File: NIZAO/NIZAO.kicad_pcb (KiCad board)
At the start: 4 copper layers, 107 x 87.7 mm, 180 parts, among them J1 Screw_Terminal_01x09, J2 Screw_Terminal_01x09, J3 Screw_Terminal_01x09, J4 Screw_Terminal_01x09, J5 PZ254R-12-14P, K1 G5V-1, K2 G5V-1, Q1 NCE60P04R, Q2 ZXMS6004FFQTA, Q3 ZXMS6004FFQTA, Q4 ZXMS6004FFQTA, Q5 ZXMS6004FFQTA, SW1 TS-1088-AR02016, U1 ADS1115IDGS, U10 AT3H4B-CUH-S, U11 MAX31856MUD+, U12 BL0942, U13 B0303S-1WR3_C7465185, U14 ISO7021DR, U15 GP8211S-TC50-EW, U16 GP8302-TC50-EW, U17 BTS723GWXUMA1, U18 LK1802, U2 ESP32-S3-WROOM-1, U3 RS485-PROTECT, U4 AP63203WU, U5 AT3H4B-CUH-S, U6 AT3H4B-CUH-S, U7 AT3H4B-CUH-S, U8 AT3H4B-CUH-S, U9 AT3H4B-CUH-S

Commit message: actualizado
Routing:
- net /BoardNIZAO/OUT_RLY2: track 12.3 -> 14.6 mm, vias 0 -> 2
- net /BoardNIZAO/IN_NPN1: track 116.2 -> 117.4 mm, vias 2 -> 0
- net /BoardNIZAO/cs: track 80.1 -> 79.0 mm
- net /BoardNIZAO/OUT_PNP2: track 33.7 -> 32.6 mm, vias 0 -> 2
- net /BoardNIZAO/IN_NPN4: track 105.6 -> 106.5 mm
- net /BoardNIZAO/OUT_NPN4: track 57.7 -> 56.9 mm, vias 2 -> 0
- net /BoardNIZAO/OUT_NPN1: track 60.1 -> 60.9 mm, vias 2 -> 0
- net /BoardNIZAO/OUT_NPN2: track 58.5 -> 59.0 mm, vias 2 -> 0
- net /BoardNIZAO/OUT_PNP1: vias 0 -> 2
- net /BoardNIZAO/OUT_NPN3: vias 2 -> 0

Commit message: actualizacion
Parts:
- moved C8 4.52 mm to (102.4, 85.3)
- moved L1 2.38 mm to (105.9, 79.9)
- moved J1 0.22 mm to (108.7, 59.8)
- moved J2 0.15 mm to (154.5, 59.7)
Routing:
- net /PawerSupply/sw: track 8.49 -> 10.1 mm
- net Net-(U4-BST): track 14.0 -> 13.2 mm
- net +3.3V: vias 42 -> 52
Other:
- board size 107 x 87.7 mm -> 102 x 82.8 mm

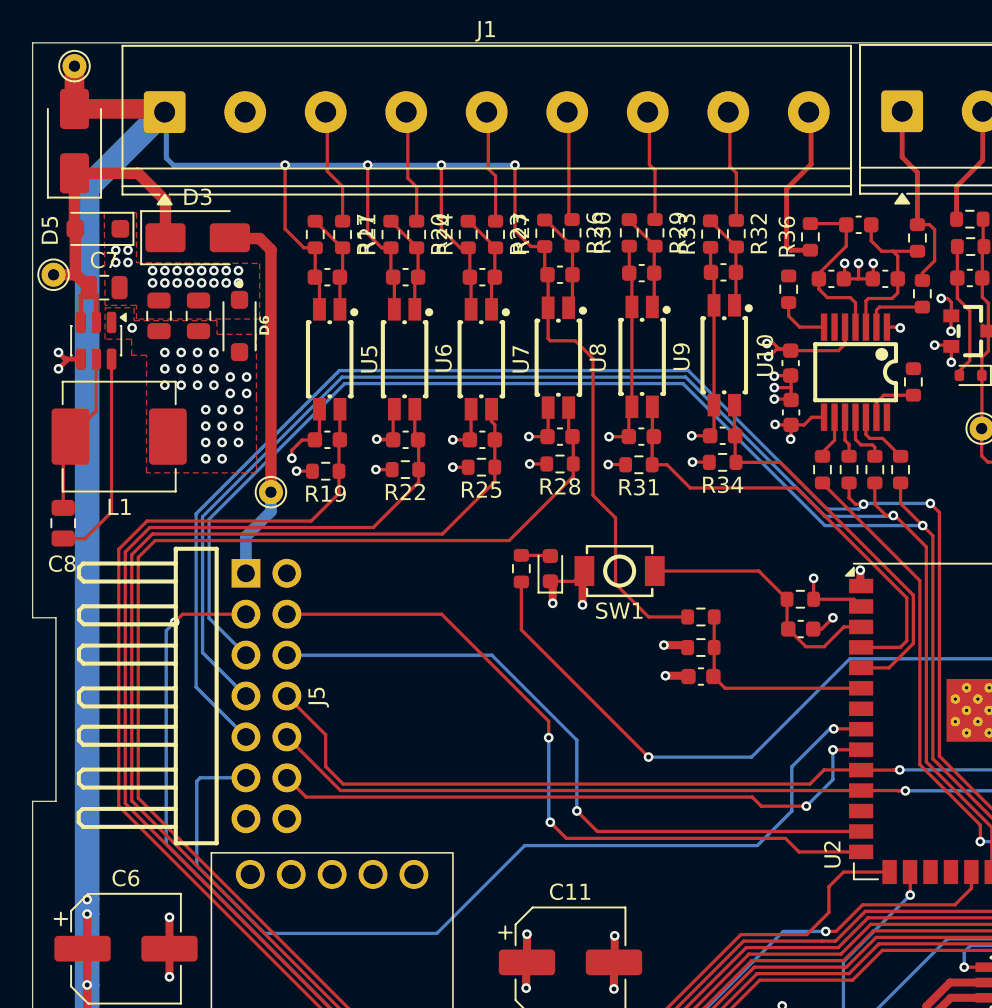
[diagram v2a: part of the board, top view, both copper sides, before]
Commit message: Actualiza el mezzanine, eliminar assembly de prueba y actualizar essembly
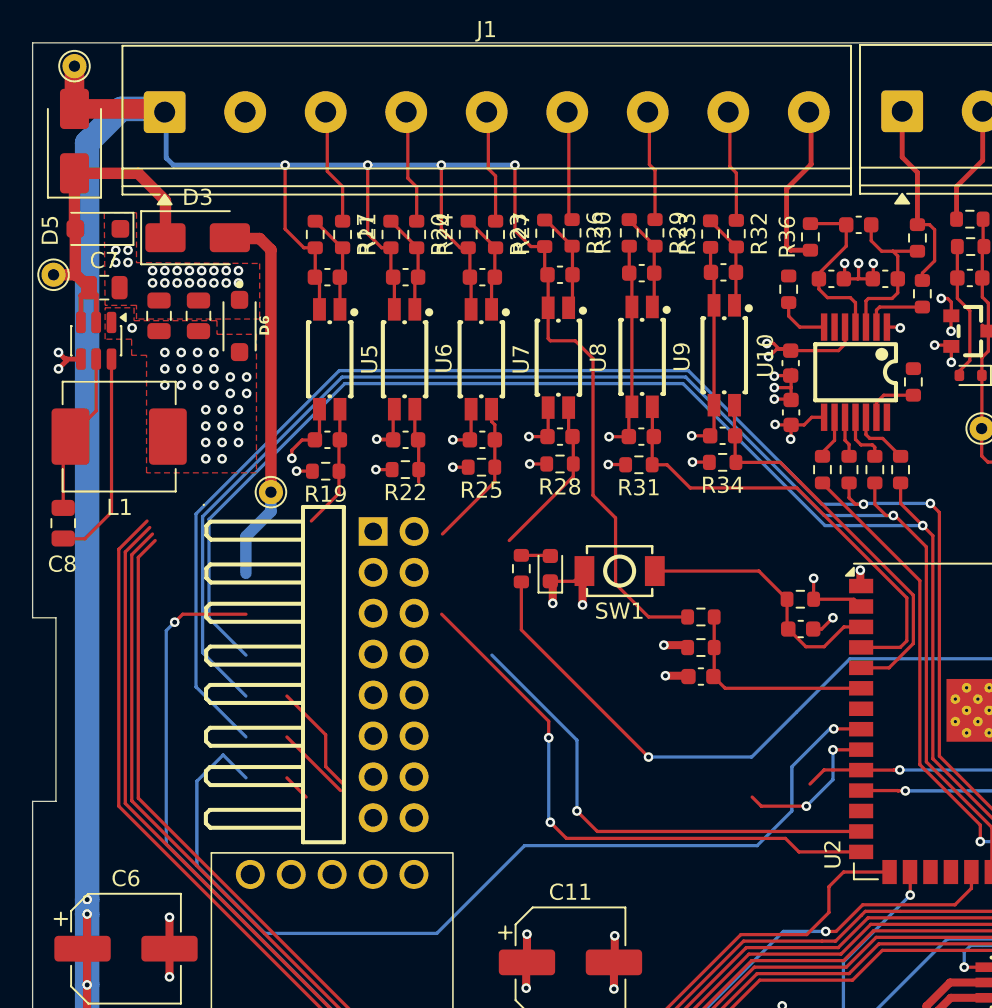
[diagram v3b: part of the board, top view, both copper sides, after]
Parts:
- removed J5: PZ254R-12-14P, XFCN PZ254R-12-14P:HDR-TH_14P-P2.54-H-M-R2-C7-S2.54
- added H3: PZ254R-12-16P, EasyEDA:HDR-TH_16P-P2.54-H-M-R2-C8-S2.54, F.Cu at (122.9, 94.7)
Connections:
- C17 pad 1: Net-(C17-Pad1) -> Net-(U19-AN/CAT)
- C19 pad 1: Net-(C19-Pad1) -> Net-(U20-AN/CAT)
- C21 pad 1: Net-(C21-Pad1) -> Net-(U21-AN/CAT)
- C23 pad 1: Net-(C23-Pad1) -> Net-(U22-AN/CAT)
- C25 pad 1: Net-(C25-Pad1) -> Net-(U23-AN/CAT)
- C27 pad 1: Net-(C27-Pad1) -> Net-(U24-AN/CAT)
- R17 pad 2: Net-(C17-Pad1) -> Net-(U19-AN/CAT)
- R18 pad 2: Net-(C17-Pad1) -> Net-(U19-AN/CAT)
- R20 pad 2: Net-(C19-Pad1) -> Net-(U20-AN/CAT)
- R21 pad 2: Net-(C19-Pad1) -> Net-(U20-AN/CAT)
- R23 pad 2: Net-(C21-Pad1) -> Net-(U21-AN/CAT)
- R24 pad 2: Net-(C21-Pad1) -> Net-(U21-AN/CAT)
- R26 pad 2: Net-(C23-Pad1) -> Net-(U22-AN/CAT)
- R27 pad 2: Net-(C23-Pad1) -> Net-(U22-AN/CAT)
- R29 pad 2: Net-(C25-Pad1) -> Net-(U23-AN/CAT)
- R30 pad 2: Net-(C25-Pad1) -> Net-(U23-AN/CAT)
- R32 pad 2: Net-(C27-Pad1) -> Net-(U24-AN/CAT)
- R33 pad 2: Net-(C27-Pad1) -> Net-(U24-AN/CAT)
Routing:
- net /BoardNIZAO/i2c_scl: track 120.9 -> 88.6 mm
- net /BoardNIZAO/i2c_sda: track 122.0 -> 93.1 mm
- net /BoardNIZAO/GPIO2: track 38.9 -> 11.2 mm
- net /BoardNIZAO/IN_NPN4: track 106.5 -> 84.5 mm
- net /BoardNIZAO/IN_NPN3: track 143.2 -> 125.1 mm
- net /BoardNIZAO/IN_NPN2: track 142.1 -> 124.2 mm
- net /BoardNIZAO/usb-: track 42.8 -> 30.0 mm
- net /BoardNIZAO/IN_NPN1: track 117.4 -> 107.2 mm
- net /BoardNIZAO/usb+: track 45.4 -> 35.8 mm
- net +24V: track 354.0 -> 355.6 mm
- net /BoardNIZAO/GPIO1: track 58.2 -> 59.4 mm

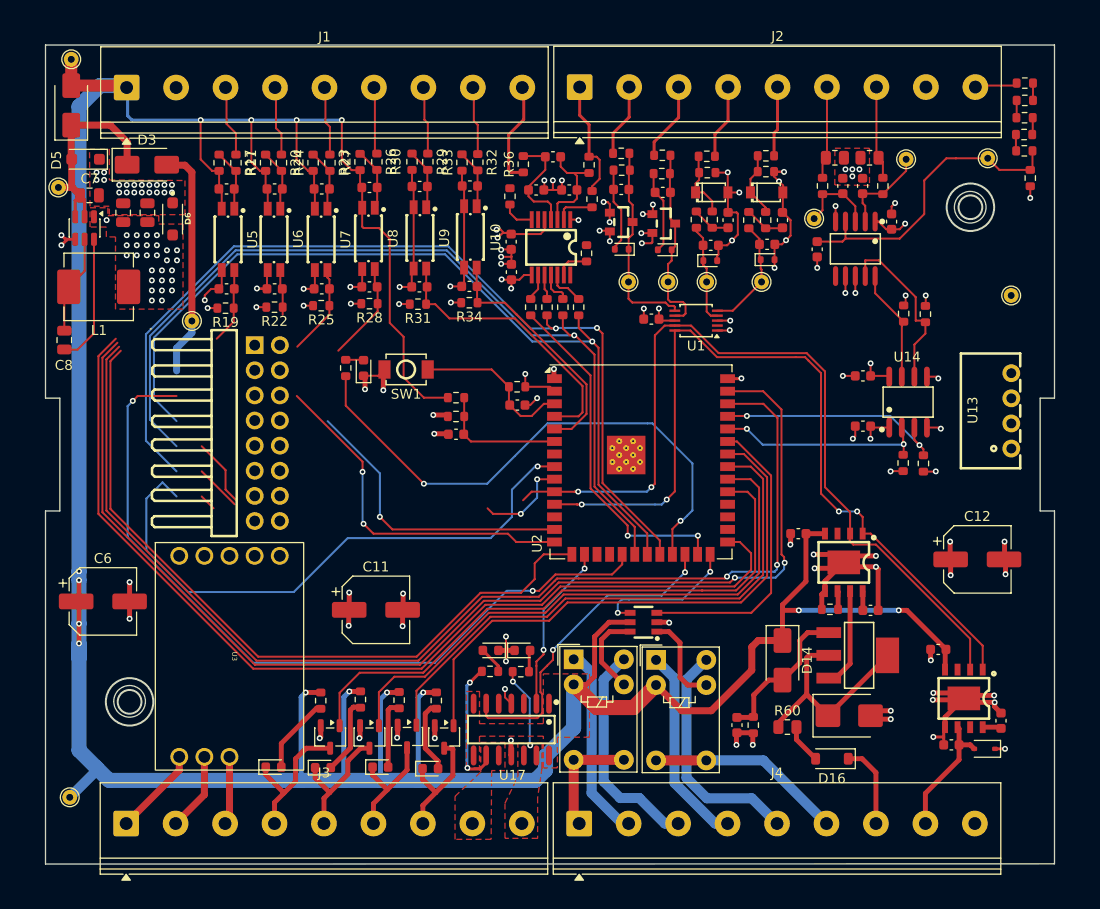
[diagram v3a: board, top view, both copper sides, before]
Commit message: Colocandos los 3d de los componetes en la placa NIZAO
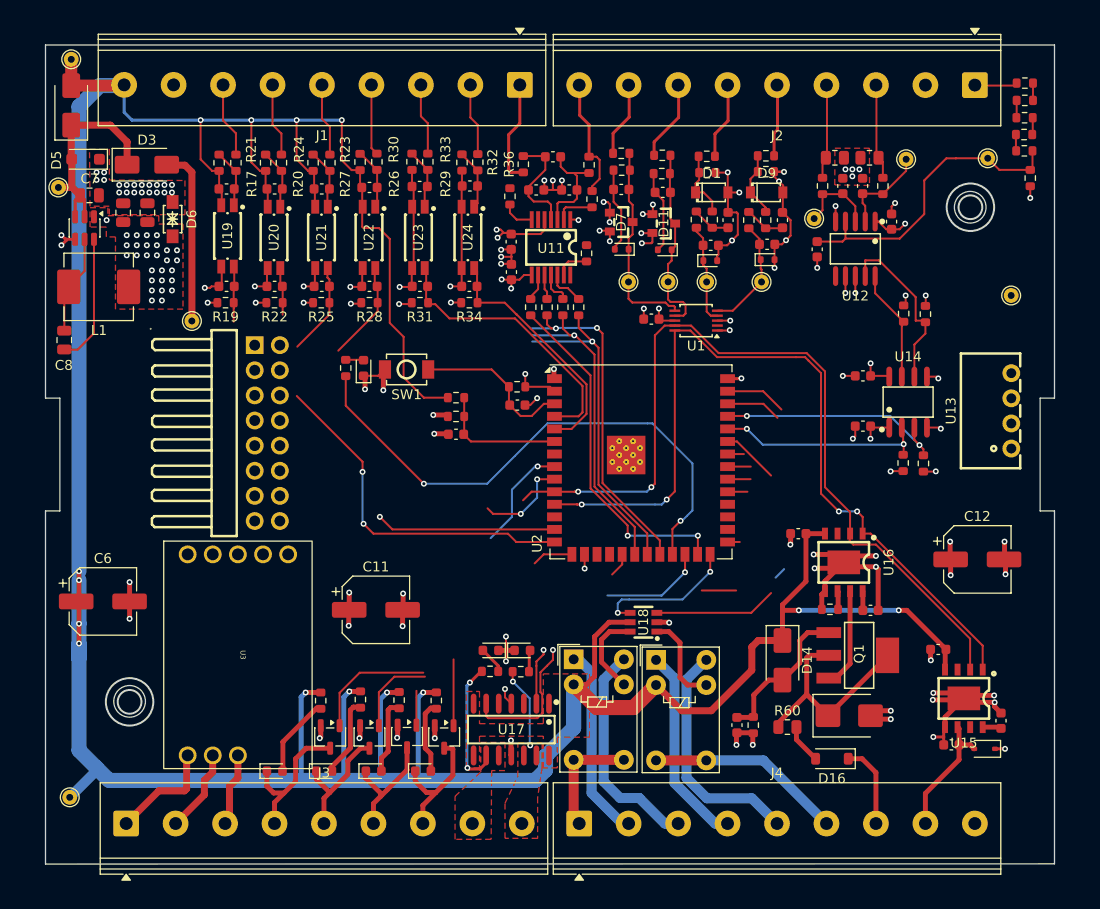
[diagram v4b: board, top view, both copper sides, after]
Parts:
- removed U10, U5, U6, U7, U8, U9: AT3H4B-CUH-S, AOTE AT3H4B-CuH-S:SSOP-4_L2.7-W4.6-P1.27-LS7.0-TL
- added U19: AT3H4B-CUH-S, JLCImport:AT3H4B-CUH-S, F.Cu at (118.9, 74.8)
- added U20: AT3H4B-CUH-S, JLCImport:AT3H4B-CUH-S, F.Cu at (123.6, 74.9)
- added U21: AT3H4B-CUH-S, JLCImport:AT3H4B-CUH-S, F.Cu at (128.4, 74.9)
- added U22: AT3H4B-CUH-S, JLCImport:AT3H4B-CUH-S, F.Cu at (133.2, 74.9)
- added U23: AT3H4B-CUH-S, JLCImport:AT3H4B-CUH-S, F.Cu at (138.2, 74.9)
- added U24: AT3H4B-CUH-S, JLCImport:AT3H4B-CUH-S, F.Cu at (143.2, 74.9)
- D1, D9: footprint DIODES 1N5819HW-7-F:SOD-123_L2.7-W1.6-LS3.7-RD -> JLCImport:1N5819HW-7-F
- D11, D7: footprint DIODES BAT54S-7-F:SOT-23_L2.9-W1.3-P1.90-LS2.4-BR -> JLCImport:BAT54S-7-F
- D6: footprint SMF3.3_SODFL3718X108N:SMF3.3_SODFL3718X108N -> JLCImport:SMF3_3CA_C6165153
- Q1: footprint NCE NCE60P04R:SOT-223-3_L6.5-W3.4-P2.30-LS7.0-BR -> JLCImport:NCE60P04R
- SW1: footprint XUNPU TS-1088-AR02016:SW-SMD_L3.9-W3.0-P4.45 -> JLCImport:TS-1088-AR02016
- U11: footprint MAXIM MAX31856MUD+:TSSOP-14_L5.0-W4.4-P0.65-LS6.4-BL -> JLCImport:MAX31856MUD
- U12: footprint BL BL0942:SSOP-10_L4.9-W3.9-P1.00-LS6.0-BL -> JLCImport:BL0942
- U13: footprint EVISUN B0303S-1WR3:PWRM-TH_BXXXXS-1WR3 -> JLCImport:B0303S-1WR3_C7465185
- U14: footprint TI ISO7021DR:SOIC-8_L4.9-W3.9-P1.27-LS6.0-BL -> JLCImport:ISO7021DR
- U15: footprint Guestgood GP8211S-TC50-EW:ESOP-8_L4.9-W3.9-P1.27-LS6.0-BL-EP -> JLCImport:GP8211S-TC50-EW
- U16: footprint Guestgood GP8211S-TC50-EW:ESOP-8_L4.9-W3.9-P1.27-LS6.0-BL-EP -> JLCImport:GP8302-TC50-EW
- U17: footprint Infineon BTS723GW:SOIC-14_L8.7-W3.9-P1.27-LS6.0-BL -> JLCImport:BTS723GWXUMA1
- U18: footprint LANKE LK1802:SOT-23-6_L2.9-W1.6-P0.95-LS2.8-BR -> JLCImport:LK1802
- moved J2 40.0 mm to (194.4, 59.5), turned to 180 degrees
- moved J1 39.8 mm to (148.4, 59.5), turned to 180 degrees
- moved U3 0.86 mm to (120.0, 117.1)
- moved LED6 0.79 mm to (133.7, 128.8)
- moved LED7 0.77 mm to (138.7, 128.8)
- moved R19 0.55 mm to (118.7, 81.5)
- moved R22 0.45 mm to (123.7, 81.5)
- moved LED4 0.42 mm to (123.7, 128.8)
- moved LED5 0.37 mm to (128.7, 128.8)
- moved R25 0.30 mm to (128.4, 81.5)
- moved C18 0.25 mm to (118.8, 79.8)
- moved C20 0.25 mm to (123.7, 79.8)
- moved C22 0.25 mm to (128.4, 79.8)
- moved R31 0.25 mm to (138.3, 81.5)
- moved R28 0.10 mm to (133.2, 81.5)
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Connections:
- J1 pad 1: +24V -> /BoardNIZAO/CON_IN_TC+
- J1 pad 2: GND -> /BoardNIZAO/CON_IN_PNP2
- J1 pad 3: /BoardNIZAO/CON_IN_NPN1 -> /BoardNIZAO/CON_IN_PNP1
- J1 pad 4: /BoardNIZAO/CON_IN_NPN2 -> /BoardNIZAO/CON_IN_NPN4
- J1 pad 6: /BoardNIZAO/CON_IN_NPN4 -> /BoardNIZAO/CON_IN_NPN2
- J1 pad 7: /BoardNIZAO/CON_IN_PNP1 -> /BoardNIZAO/CON_IN_NPN1
- J1 pad 8: /BoardNIZAO/CON_IN_PNP2 -> GND
- J1 pad 9: /BoardNIZAO/CON_IN_TC+ -> +24V
- J2 pad 1: /BoardNIZAO/CON_IN_TC- -> /BoardNIZAO/CON-IN_VAC_P
- J2 pad 2: /BoardNIZAO/CON_IN_0-10V_1 -> Earth
- J2 pad 3: /BoardNIZAO/CON_IN_0-10V_2 -> /BoardNIZAO/CON-IN_CT_P
- J2 pad 4: /BoardNIZAO/CON-IN-4-20MA_1 -> /BoardNIZAO/CON-IN_CT_N
- J2 pad 6: /BoardNIZAO/CON-IN_CT_N -> /BoardNIZAO/CON-IN-4-20MA_1
- J2 pad 7: /BoardNIZAO/CON-IN_CT_P -> /BoardNIZAO/CON_IN_0-10V_2
- J2 pad 8: Earth -> /BoardNIZAO/CON_IN_0-10V_1
- J2 pad 9: /BoardNIZAO/CON-IN_VAC_P -> /BoardNIZAO/CON_IN_TC-
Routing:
- net /BoardNIZAO/IN_NPN2: track 124.2 -> 12.1 mm, vias 2 -> 0
- net /BoardNIZAO/IN_NPN3: track 125.1 -> 14.8 mm, vias 2 -> 0
- net /BoardNIZAO/IN_NPN1: track 107.2 -> 6.49 mm
- net /BoardNIZAO/cs: track 79.0 -> 2.46 mm, vias 2 -> 0
- net /BoardNIZAO/IN_NPN4: track 84.5 -> 14.2 mm
- net /BoardNIZAO/clk: track 95.4 -> 34.3 mm
- net /BoardNIZAO/miso: track 89.8 -> 31.8 mm
- net /BoardNIZAO/mosi: track 87.9 -> 33.1 mm
- net /BoardNIZAO/OUT_NPN3: track 57.2 -> 5.83 mm
- net /BoardNIZAO/OUT_NPN4: track 56.9 -> 8.36 mm
- net /BoardNIZAO/GPIO1: track 59.4 -> 11.1 mm
- net /BoardNIZAO/OUT_NPN2: track 59.0 -> 11.0 mm
- net /BoardNIZAO/OUT_NPN1: track 60.9 -> 18.1 mm
- net /BoardNIZAO/OUT_RLY1: track 30.1 -> 18.2 mm
- net /BoardNIZAO/usb-: track 30.0 -> 18.2 mm
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- added copper zone on In2.Cu, net +3.3V
- added copper zone on In1.Cu, net GND
- removed copper zone on In1.Cu, net +3.3V
- removed copper zone on In2.Cu, net GND

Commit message: atualizando
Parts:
- H3: footprint EasyEDA:HDR-TH_16P-P2.54-H-M-R2-C8-S2.54 -> EasyEDA:HDR-TH_16P-P2.54-H-M-R2-C8-S2.542
- moved TP6 2.50 mm to (115.3, 85.8)
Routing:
- net /BoardNIZAO/cs: track 2.46 -> 85.2 mm, vias 0 -> 3
- net /BoardNIZAO/mosi: track 33.1 -> 101.4 mm, vias 1 -> 7
- net /BoardNIZAO/miso: track 31.8 -> 99.9 mm, vias 1 -> 7
- net /BoardNIZAO/IN_NPN1: track 6.49 -> 72.6 mm, vias 0 -> 2
- net /BoardNIZAO/clk: track 34.3 -> 98.3 mm, vias 2 -> 7
- net /BoardNIZAO/OUT_NPN3: track 5.83 -> 63.5 mm, vias 0 -> 4
- net /BoardNIZAO/OUT_NPN4: track 8.36 -> 57.2 mm, vias 0 -> 2
- net /BoardNIZAO/OUT_NPN2: track 11.0 -> 59.5 mm, vias 0 -> 2
- net /BoardNIZAO/IN_NPN2: track 12.1 -> 54.0 mm, vias 0 -> 2
- net /BoardNIZAO/OUT_NPN1: track 18.1 -> 58.6 mm, vias 0 -> 4
- net /BoardNIZAO/IN_NPN3: track 14.8 -> 52.1 mm, vias 0 -> 2
- net /BoardNIZAO/IN_NPN4: track 14.2 -> 48.4 mm, vias 0 -> 2
- net /BoardNIZAO/i2c_scl: track 83.9 -> 115.9 mm, vias 4 -> 7
- net /BoardNIZAO/i2c_sda: track 86.1 -> 117.7 mm, vias 2 -> 5
- net /BoardNIZAO/usb-: track 18.2 -> 38.9 mm, vias 1 -> 3
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
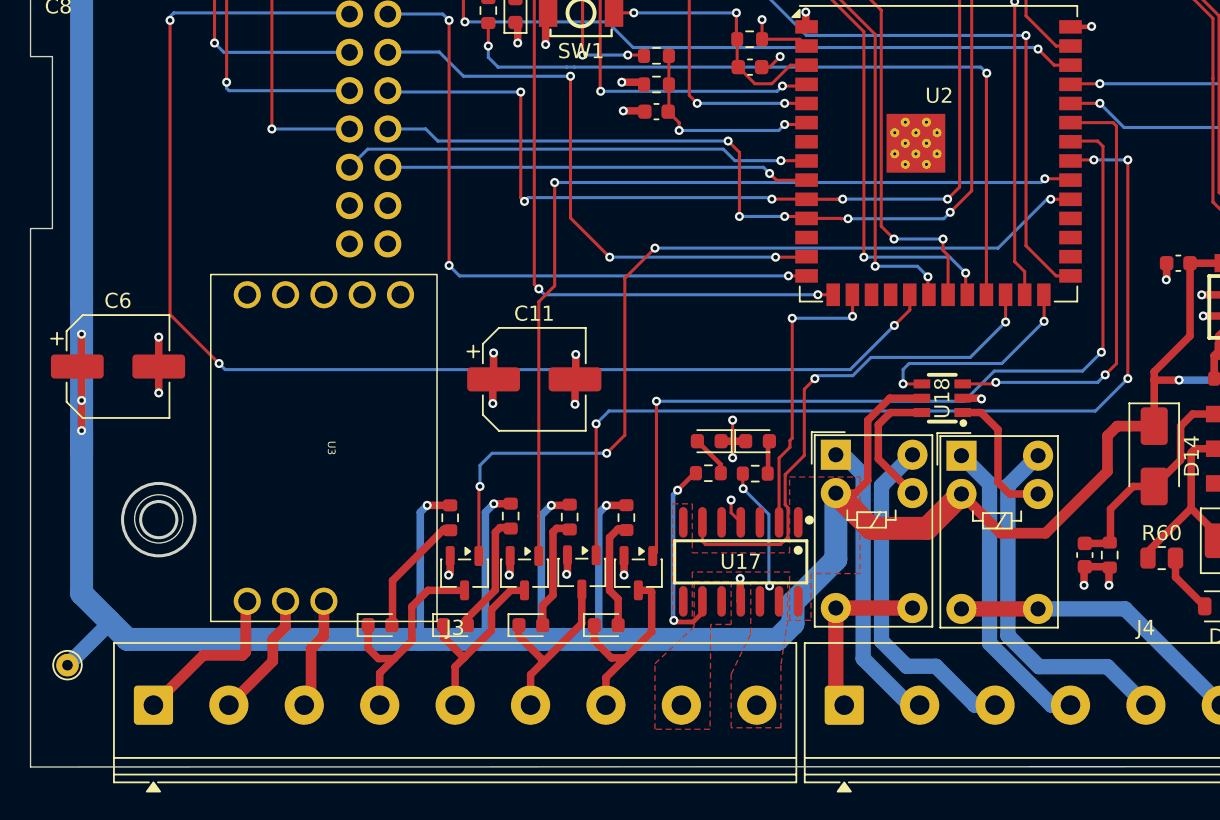
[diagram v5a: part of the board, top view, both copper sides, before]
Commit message: ACtualizandos las medidad del case de plastico y NIZAO
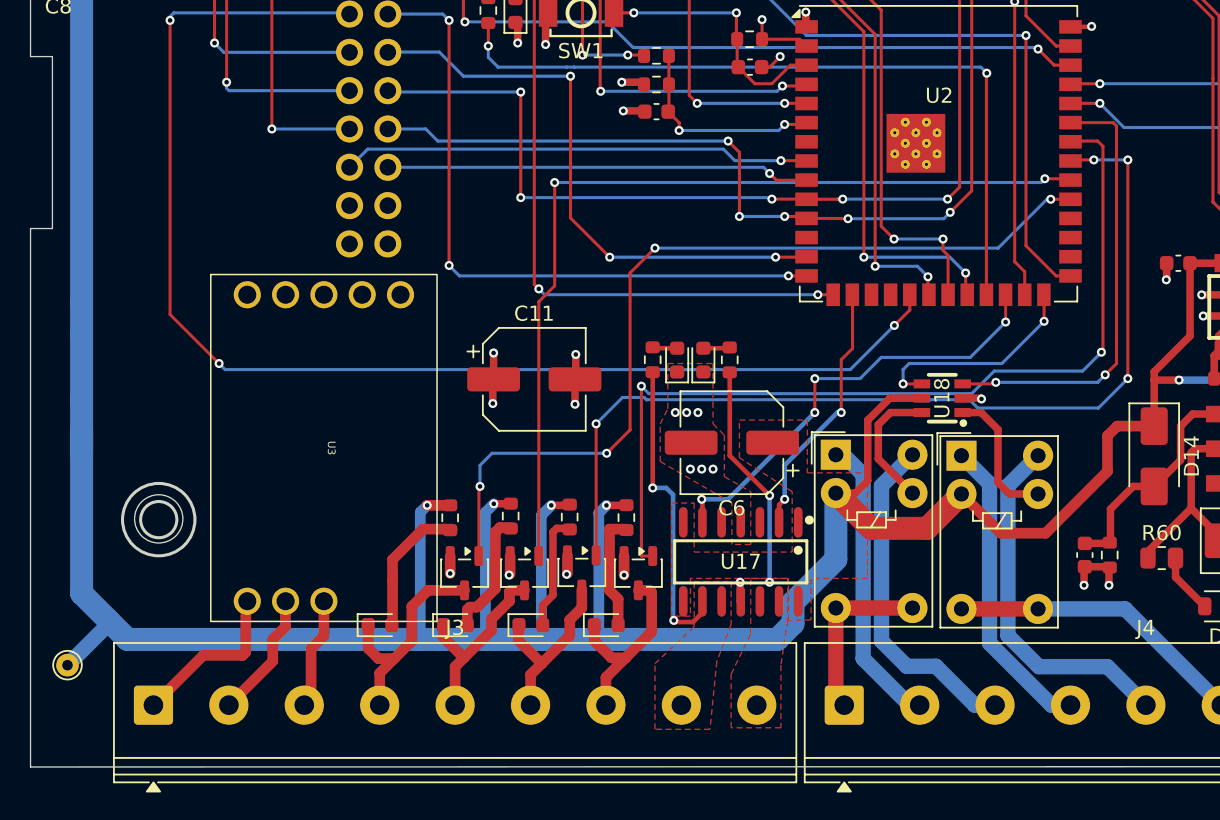
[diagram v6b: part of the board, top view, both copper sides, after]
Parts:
- moved C6 41.0 mm to (147.0, 116.8), turned to 180 degrees
- moved R62 8.38 mm to (141.8, 111.2), turned to 90 degrees
- moved R61 7.73 mm to (146.9, 111.3), turned to 90 degrees
- moved LED2 6.47 mm to (145.1, 111.3), turned to 90 degrees
- moved LED3 5.78 mm to (143.4, 111.3), turned to 90 degrees
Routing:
- net GND: track 179.0 -> 169.2 mm, vias 87 -> 88
- net /BoardNIZAO/CON_OUT_PNP_1: track 13.4 -> 20.5 mm
- net /BoardNIZAO/CON_OUT_PNP_2: track 8.19 -> 15.1 mm
- net +24V: track 356.4 -> 349.8 mm, vias 15 -> 12
- net /BoardNIZAO/OUT_PNP2: track 34.6 -> 29.7 mm, vias 2 -> 4
- net /BoardNIZAO/OUT_NPN4: track 57.2 -> 59.9 mm
- net /BoardNIZAO/OUT_PNP1: track 19.4 -> 17.5 mm
- net Net-(LED3-A): track 2.76 -> 1.65 mm
- net Net-(LED4-A): track 8.34 -> 9.15 mm
- net Net-(LED5-A): track 7.82 -> 8.41 mm
- net /BoardNIZAO/OUT_NPN3: track 63.5 -> 64.1 mm
